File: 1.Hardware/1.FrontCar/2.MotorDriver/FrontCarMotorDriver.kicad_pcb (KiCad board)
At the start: 2 copper layers, 52 parts, among them IC1 DRV8701ERGER, IC2 DRV8701ERGER, IC3 SN74LVC244APW, J1 Conn_02x03_Odd_Even, J2 Conn_01x02, J3 Conn_01x02, J4 Conn_02x03_Odd_Even, J5 Conn_02x03_Odd_Even, M1 Motor_DC, M2 Motor_DC, Q1 NMOS, Q2 NMOS, Q3 NMOS, Q4 NMOS, Q5 NMOS, Q6 NMOS, Q7 NMOS, Q8 NMOS, SW1 SW_SPDT, SW2 SW_SPDT

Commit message: 完成板子形状设计
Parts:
- added REF**: MountingHole_3.2mm_M3_Pad_Via, MountingHole:MountingHole_3.2mm_M3_Pad_Via, F.Cu at (121.5, 28.0)
- added REF**: MountingHole_3.2mm_M3_Pad_Via, MountingHole:MountingHole_3.2mm_M3_Pad_Via, F.Cu at (13.5, 28.0)
- moved D1 248.9 mm to (47.0, 5.65)
- moved C1 248.9 mm to (41.4, 11.7)
- moved C11 248.9 mm to (46.9, 8.38)
- moved C2 248.9 mm to (27.4, 19.8)
- moved C5 248.9 mm to (32.4, 18.9)
- moved C7 248.9 mm to (32.4, 21.4)
- moved C9 248.9 mm to (36.4, 18.0)
- moved IC1 248.9 mm to (36.2, 13.6)
- moved Q1 248.9 mm to (20.2, 19.5)
- moved Q3 248.9 mm to (40.8, 7.37)
- moved Q5 248.9 mm to (28.9, 14.6)
- moved Q7 248.9 mm to (32.5, 7.37)
- moved R1 248.9 mm to (20.4, 13.9)
- moved M1 240.4 mm to (9.93, 47.1)
- moved C14 195.5 mm to (44.8, -10.0)
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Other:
- board outline added: 135 x 113 mm

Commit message: 。。？
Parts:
- moved D? 87.3 mm to (20.3, 79.3), turned to 90 degrees
- moved R? 83.2 mm to (10.1, 71.1)
- moved C14 59.0 mm to (103.7, -7.07), turned to 90 degrees
- moved U? 58.6 mm to (95.4, -8.69), turned to 90 degrees
- moved C? 51.6 mm to (100.6, -6.31), turned to 90 degrees
- moved C? 47.9 mm to (90.3, -6.32), turned to 90 degrees
- moved C17 43.0 mm to (87.2, -7.09), turned to 90 degrees
- moved C10 34.2 mm to (86.0, 19.0), turned to -90 degrees
- moved J1 31.9 mm to (120.7, 0.00)
- moved J4 31.9 mm to (17.3, 0.00)
- moved C12 27.2 mm to (86.0, 15.5), turned to 90 degrees
- moved Q8 22.5 mm to (114.3, 18.5), turned to 180 degrees
- moved D2 21.5 mm to (98.0, 12.0), turned to -90 degrees
- moved C8 18.4 mm to (88.1, 12.0), turned to -90 degrees
- moved IC2 18.1 mm to (90.0, 17.0), turned to -90 degrees
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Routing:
- net Net-(D4-Pad2): track 0.00 -> 17.1 mm
- net +3V3: track 0.00 -> 15.9 mm
- net Net-(D5-Pad2): track 0.00 -> 11.1 mm
- net VCC: track 0.00 -> 6.02 mm
- net /WKUP: track 0.00 -> 5.46 mm
- net /PWM2: track 0.00 -> 3.06 mm
- net /PWM1: track 0.00 -> 3.06 mm
- net /DIR2: track 0.00 -> 2.98 mm
- net /DIR1: track 0.00 -> 2.98 mm
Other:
- board text added: "EN"
- board text added: "ON OFF"
- board text added: "PWR"

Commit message: 啊啊啊啊啊啊
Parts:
- renumbered J3 to 18650x2, J1 to 7.4V, J4 to GND, M1 to LEFT, J2 to PWR, M2 to RIGHT
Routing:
- net Net-(C1-Pad2): track 0.00 -> 12.2 mm
- net Net-(C3-Pad1): track 0.00 -> 12.1 mm
- net Net-(C9-Pad1): track 0.00 -> 9.30 mm
- net Net-(C10-Pad1): track 0.00 -> 9.21 mm
- net Net-(C8-Pad1): track 0.00 -> 4.75 mm
- net Net-(C7-Pad1): track 0.00 -> 4.69 mm
- net Net-(C8-Pad2): track 0.00 -> 3.00 mm
- net Net-(C7-Pad2): track 0.00 -> 2.93 mm
- net Net-(C6-Pad2): track 0.00 -> 2.64 mm
- net Net-(C5-Pad2): track 0.00 -> 2.56 mm
- net Net-(C11-Pad1): track 0.00 -> 2.14 mm
- net Net-(C12-Pad1): track 0.00 -> 2.09 mm

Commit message: ？
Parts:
- moved IC3 55.3 mm to (67.7, 28.0), turned to 0 degrees
- moved C? 52.9 mm to (73.3, 25.9), turned to -90 degrees
- moved LEFT 0.31 mm to (13.0, 46.5)
- moved RIGHT 0.23 mm to (121.7, 46.5)
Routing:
- net Net-(C13-Pad1): track 0.00 -> 16.6 mm
- net /DIR2: track 2.98 -> 3.62 mm
- added copper zone on B.Cu, net +7.5V

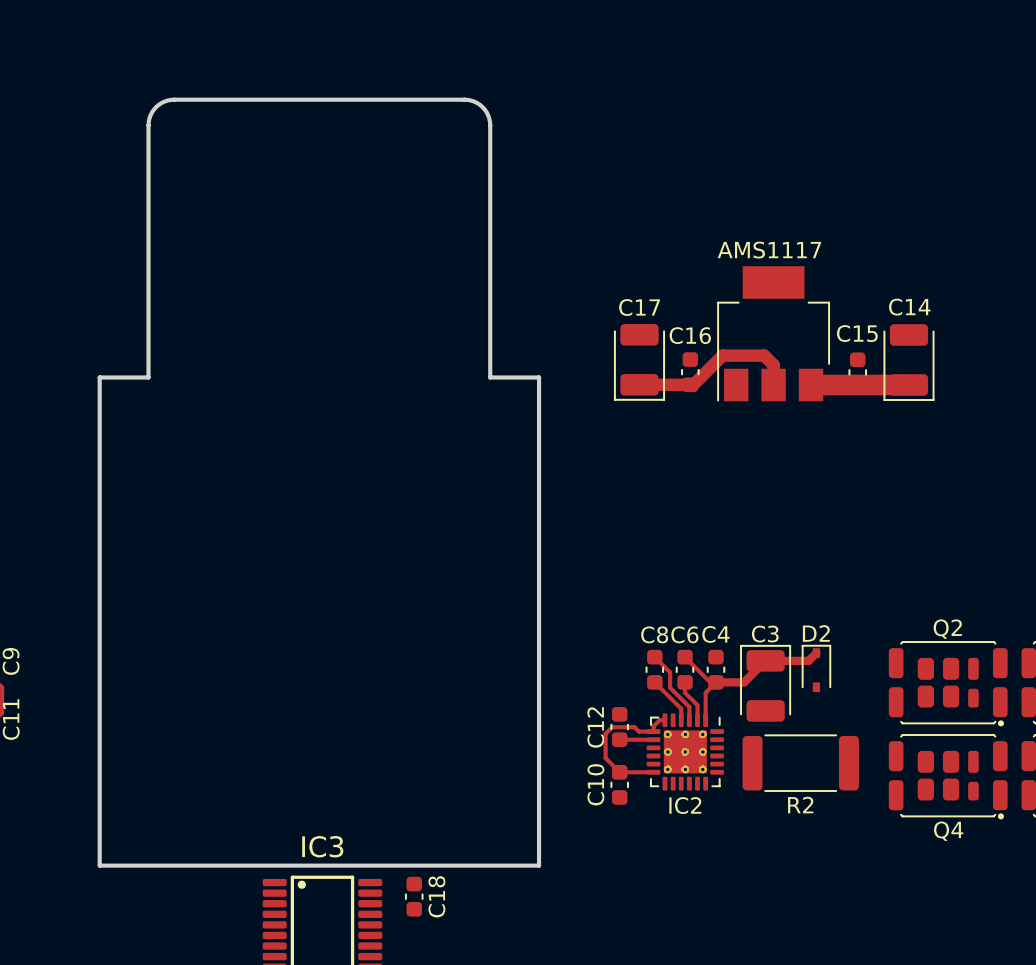
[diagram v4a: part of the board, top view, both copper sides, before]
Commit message: 增加两个外接，带按键屏幕模块
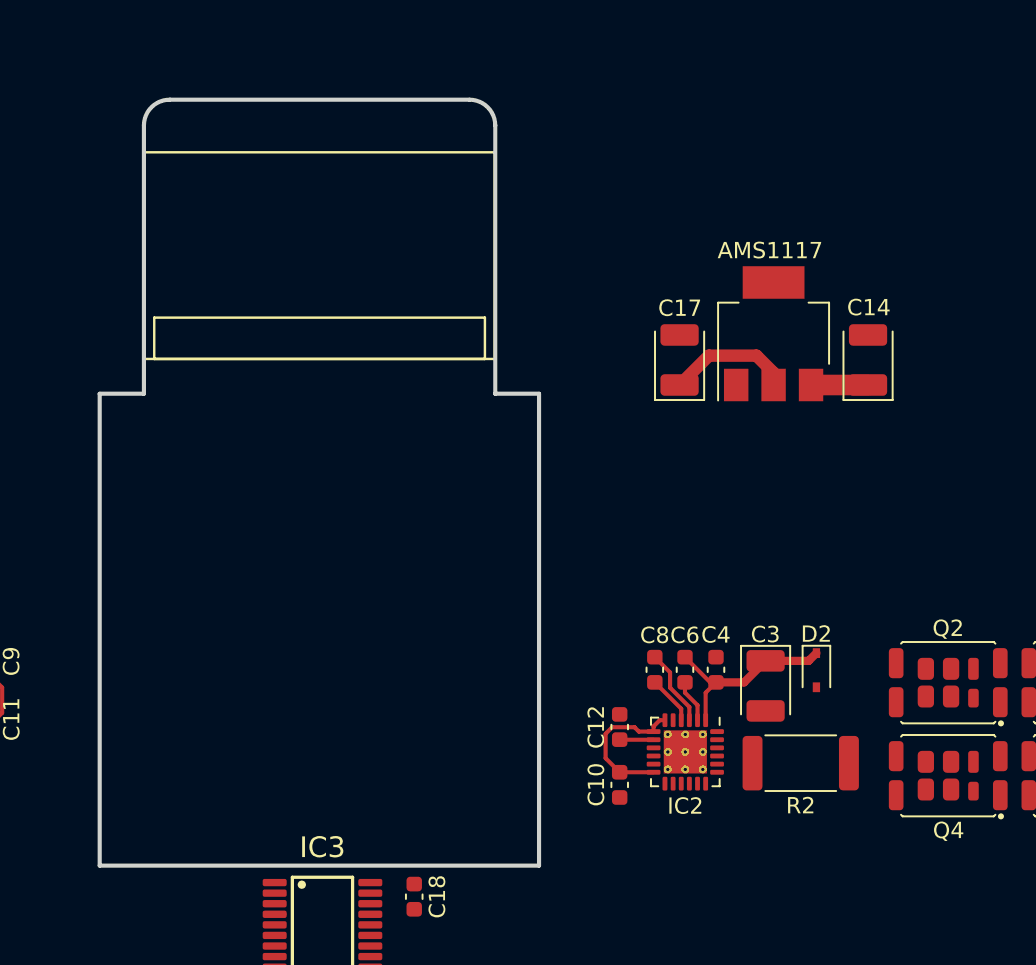
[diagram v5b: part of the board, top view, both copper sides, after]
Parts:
- removed the C? at (90.3, -6.32)
- removed the C? at (100.6, -6.31)
- moved C14 2.51 mm to (101.2, -7.07)
- moved C17 2.46 mm to (89.6, -7.07)
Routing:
- net +3V3: track 15.9 -> 13.2 mm
- net VCC: track 6.02 -> 3.51 mm
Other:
- outline, holes or cut-outs redrawn
